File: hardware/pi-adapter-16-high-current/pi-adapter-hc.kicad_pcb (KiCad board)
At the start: 4 copper layers, 70 x 56 mm, 39 parts, among them J1 Conn_02x02_Odd_Even, P1 CONN_01X04, P10 CONN_01X04, P11 CONN_01X04, P12 CONN_01X04, P13 CONN_01X04, P14 CONN_01X04, P15 CONN_01X04, P16 CONN_01X04, P17 5V, P2 CONN_01X04, P20 Pi-GPIO, P21 I2C, P22 System SPI, P23 UART, P3 CONN_01X04, P30 +5V, P31 GND, P32 +5V, P4 CONN_01X04, P40 CONN_01X01, P41 CONN_01X01, P43 CONN_01X01, P5 CONN_01X04, P6 CONN_01X04, P7 CONN_01X04, P8 CONN_01X04, P9 CONN_01X04, U1 74HC245, U2 74HC245, U3 74HC245, U4 74HC245

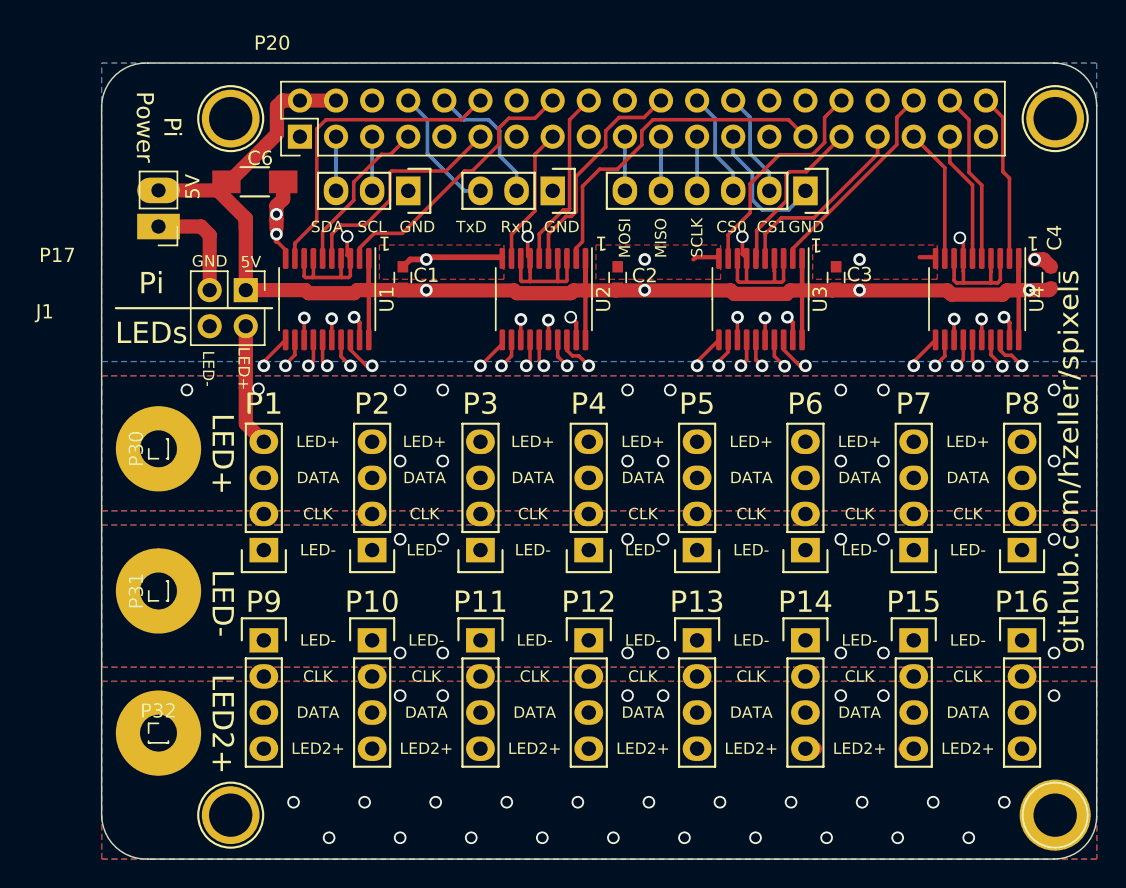
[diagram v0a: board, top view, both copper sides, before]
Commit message: Add second LED minus lug for symmetry.
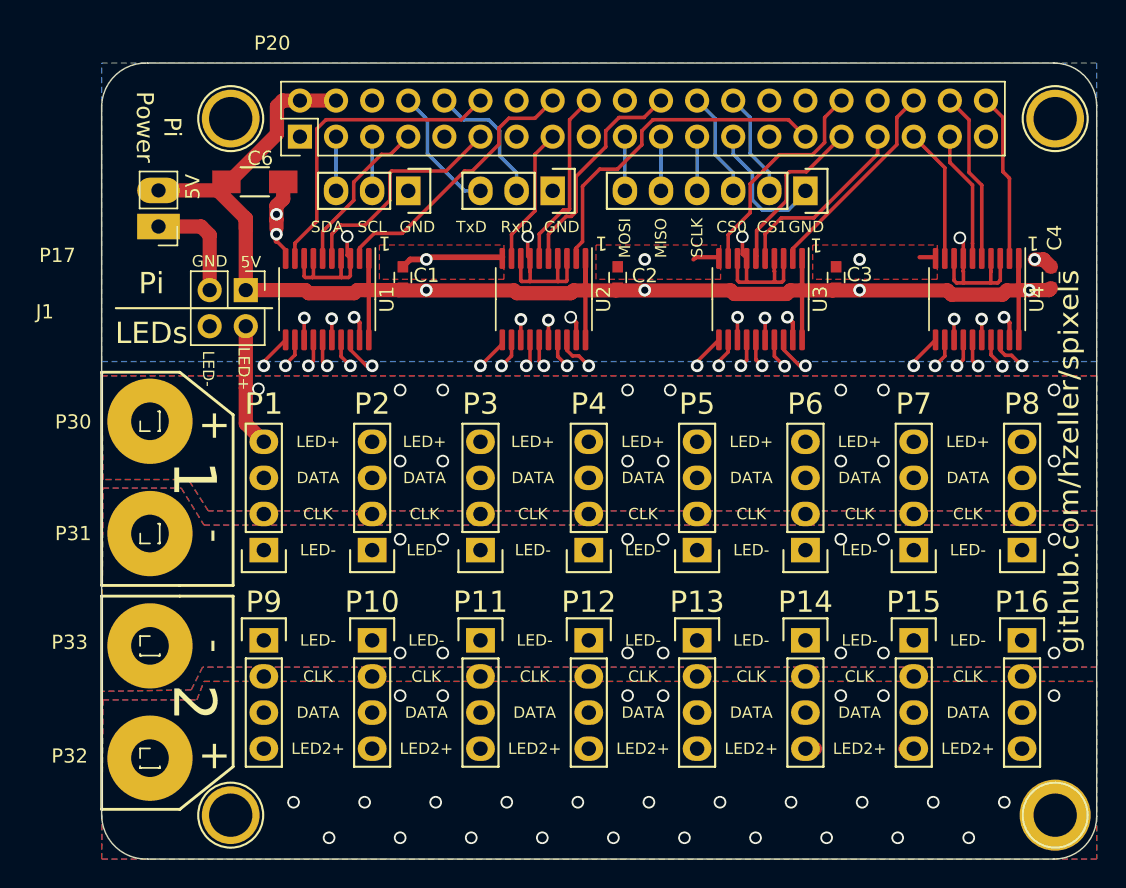
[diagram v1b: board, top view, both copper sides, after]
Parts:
- added P33: GND, Connector_PinHeader_1.00mm:PinHeader_1x01_P1.00mm_Vertical, F.Cu at (97.4, 79.0)
- moved P31 4.08 mm to (97.4, 71.1)
- moved P30 2.03 mm to (97.4, 63.2)
- moved P32 1.86 mm to (97.4, 86.9)
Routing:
- net LED-Power-: track 20.9 -> 18.1 mm
- net LED-Power+: vias 16 -> 15
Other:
- board text added: "+"
- board text added: "-"
- board text added: "2"

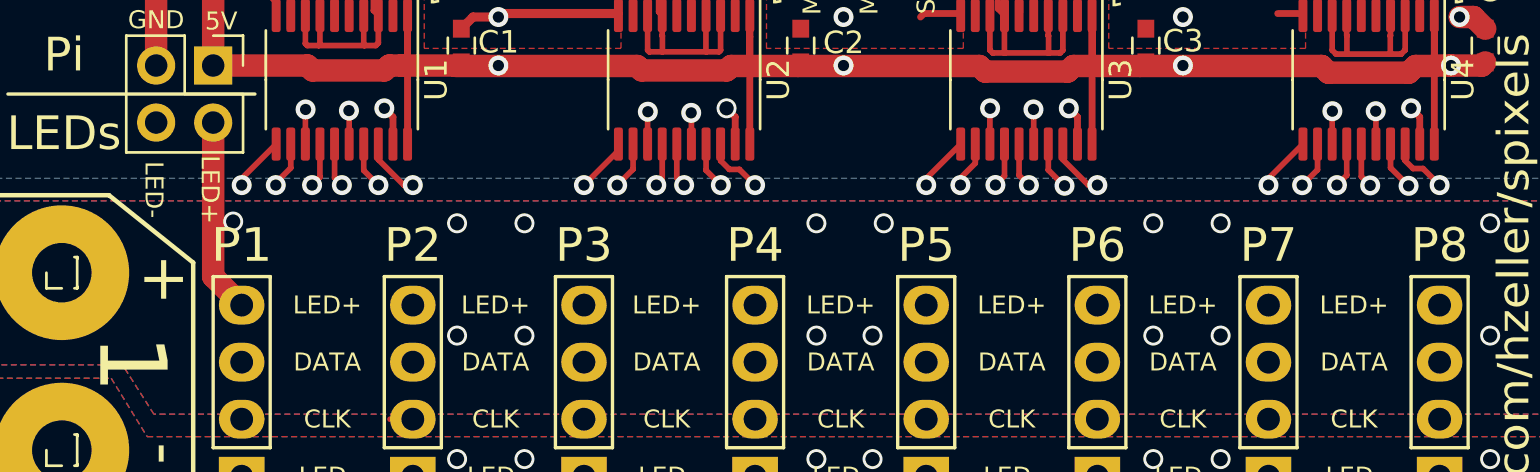
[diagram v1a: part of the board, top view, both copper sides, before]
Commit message: More clarity in naming LED1+
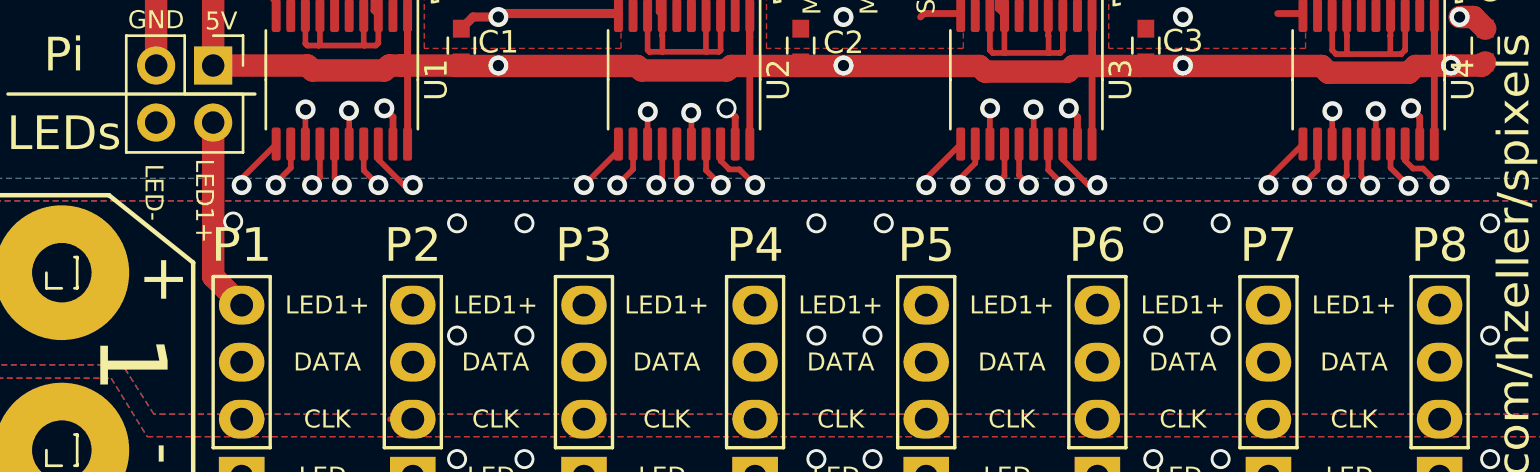
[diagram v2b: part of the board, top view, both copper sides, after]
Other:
- board text added: "LED1+"
- board text removed: "LED+"
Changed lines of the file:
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@@
     (effects (font (size 0.8 0.8) (thickness 0.15)))
   )
-  (gr_text "LED+" (at 109.22 64.643) (layer "F.SilkS")
+  (gr_text "LED1+" (at 109.22 64.643) (layer "F.SilkS")
     (effects (font (size 0.8 0.8) (thickness 0.15)))
   )
@@
     (effects (font (size 1 1) (thickness 0.25)))
   )
-  (gr_text "LED-" (at 101.5 59.5 270) (layer "F.SilkS")
+  (gr_text "LED-" (at 101.5 59.619047 270) (layer "F.SilkS")
     (effects (font (size 0.8 0.8) (thickness 0.15)))
   )
@@
     (effects (font (size 0.8 0.8) (thickness 0.15)))
   )
-  (gr_text "LED+" (at 104 59.5 270) (layer "F.SilkS")
+  (gr_text "LED1+" (at 103.75 60 270) (layer "F.SilkS")
     (effects (font (size 0.8 0.8) (thickness 0.15)))
   )
-  (gr_text "LED+" (at 116.713 64.643) (layer "F.SilkS")
+  (gr_text "LED1+" (at 116.713 64.643) (layer "F.SilkS")
     (effects (font (size 0.8 0.8) (thickness 0.15)))
   )
@@
     (effects (font (size 0.8 0.8) (thickness 0.15)))
   )
-  (gr_text "LED+" (at 154.94 64.643) (layer "F.SilkS")
+  (gr_text "LED1+" (at 154.94 64.643) (layer "F.SilkS")
     (effects (font (size 0.8 0.8) (thickness 0.15)))
   )
@@
     (effects (font (size 0.8 0.8) (thickness 0.15)))
   )
-  (gr_text "LED+" (at 147.32 64.643) (layer "F.SilkS")
+  (gr_text "LED1+" (at 147.32 64.643) (layer "F.SilkS")
     (effects (font (size 0.8 0.8) (thickness 0.15)))
   )
@@
     (effects (font (size 2 2) (thickness 0.5)))
   )
-  (gr_text "LED+" (at 124.333 64.643) (layer "F.SilkS")
+  (gr_text "LED1+" (at 124.333 64.643) (layer "F.SilkS")
     (effects (font (size 0.8 0.8) (thickness 0.15)))
   )
@@
     (effects (font (size 0.8 0.8) (thickness 0.15)))
   )
-  (gr_text "LED+" (at 132.08 64.643) (layer "F.SilkS")
+  (gr_text "LED1+" (at 132.08 64.643) (layer "F.SilkS")
     (effects (font (size 0.8 0.8) (thickness 0.15)))
   )
@@
     (effects (font (size 1.2 1.2) (thickness 0.2)))
   )
-  (gr_text "LED+" (at 139.7 64.643) (layer "F.SilkS")
+  (gr_text "LED1+" (at 139.7 64.643) (layer "F.SilkS")
     (effects (font (size 0.8 0.8) (thickness 0.15)))
   )
